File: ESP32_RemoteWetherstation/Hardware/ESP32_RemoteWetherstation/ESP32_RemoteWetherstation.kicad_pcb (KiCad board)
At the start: 2 copper layers, 48.6 x 21.9 mm, 16 parts, among them IC301 TLV77333PDBVR, J301 BOOT, J302 UART, U301 ESP32-WROOM-32E, U302 BME280

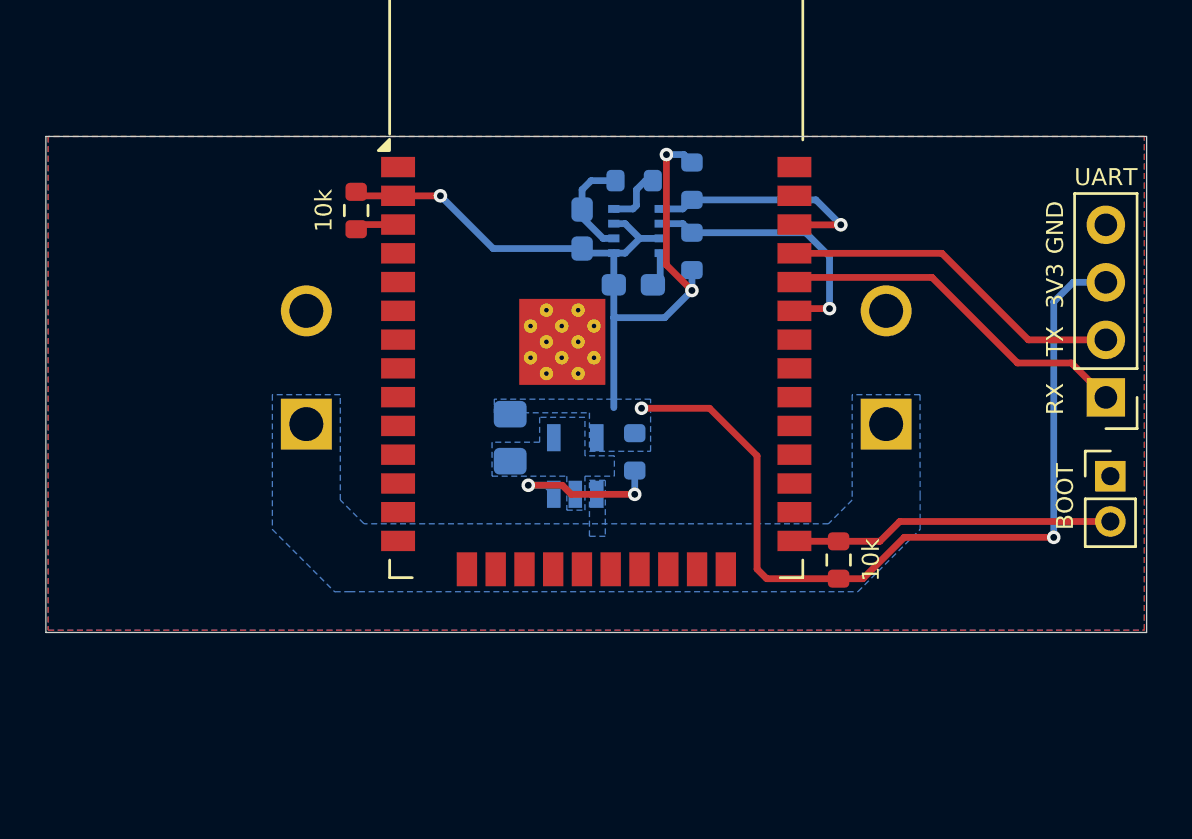
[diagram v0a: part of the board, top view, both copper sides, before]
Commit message: added IO, changed LDO
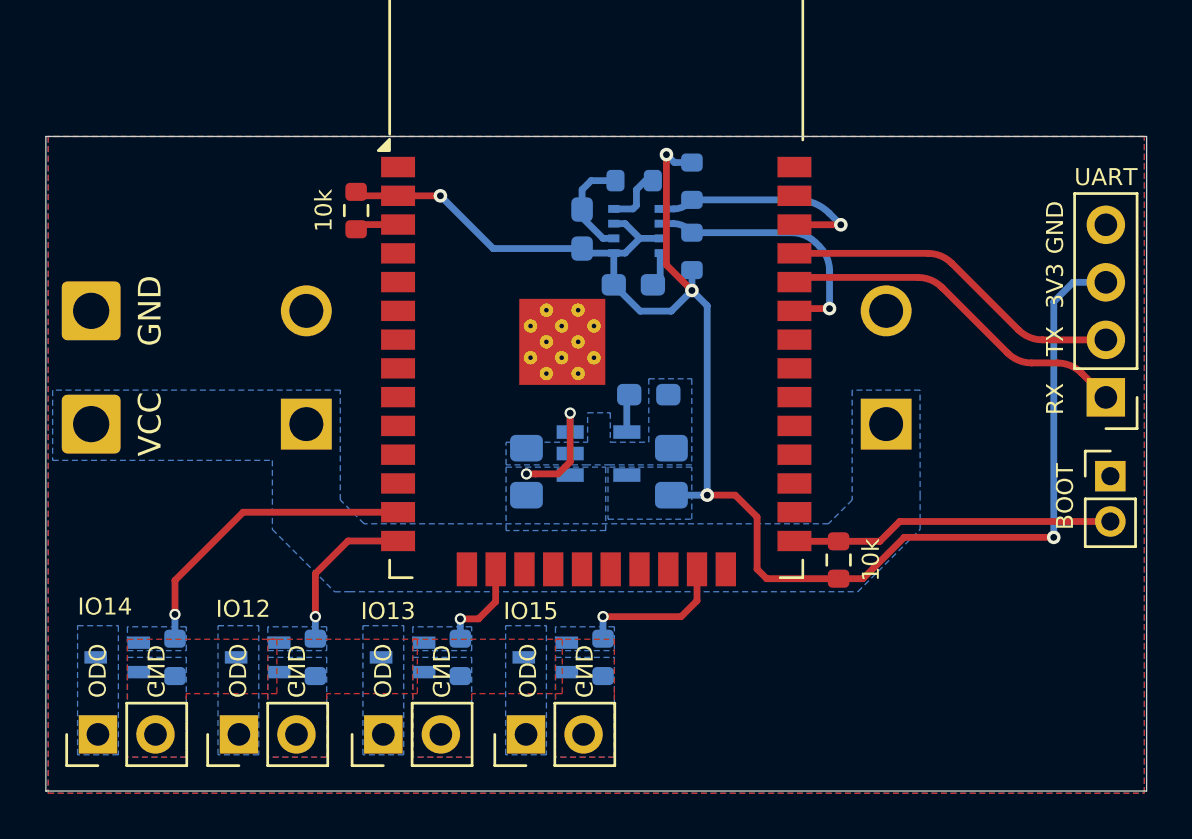
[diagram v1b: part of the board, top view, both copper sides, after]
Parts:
- removed RE_TLV301: 10k, Resistor_SMD:R_0603_1608Metric
- added C306: 1uF, Capacitor_SMD:C_0805_2012Metric_Pad1.18x1.45mm_HandSolder, B.Cu at (143.7, 65.3)
- added C307: 100pF, Capacitor_SMD:C_0603_1608Metric_Pad1.08x0.95mm_HandSolder, B.Cu at (142.7, 61.9)
- added J303: VCC, Connector_Wire:SolderWire-0.75sqmm_1x01_D1.25mm_OD2.3mm, F.Cu at (118.1, 63.2)
- added J304: GND, Connector_Wire:SolderWire-0.75sqmm_1x01_D1.25mm_OD2.3mm, F.Cu at (118.1, 58.2)
- added J305: OpenDrain, Connector_PinHeader_2.54mm:PinHeader_1x02_P2.54mm_Vertical, F.Cu at (118.4, 76.9)
- added J306: OpenDrain, Connector_PinHeader_2.54mm:PinHeader_1x02_P2.54mm_Vertical, F.Cu at (124.6, 76.9)
- added J307: OpenDrain, Connector_PinHeader_2.54mm:PinHeader_1x02_P2.54mm_Vertical, F.Cu at (131.0, 76.9)
- added J308: OpenDrain, Connector_PinHeader_2.54mm:PinHeader_1x02_P2.54mm_Vertical, F.Cu at (137.3, 76.9)
- added NT301: 0.3, Nettie_Jan:NetTie-2_SMD_Pad0.3mm, F.Cu at (138.2, 65.4)
- added Q301: NX5020UNBKWX, LibKiCad:SOT65P210X110-3N, B.Cu at (119.2, 73.5)
- added Q302: NX5020UNBKWX, LibKiCad:SOT65P210X110-3N, B.Cu at (125.5, 73.5)
- added Q303: NX5020UNBKWX, LibKiCad:SOT65P210X110-3N, B.Cu at (131.8, 73.5)
- added Q304: NX5020UNBKWX, LibKiCad:SOT65P210X110-3N, B.Cu at (138.2, 73.5)
- added R304: 100k, Resistor_SMD:R_0603_1608Metric, B.Cu at (121.8, 73.5)
- added R305: 100k, Resistor_SMD:R_0603_1608Metric, B.Cu at (128.0, 73.5)
- added R306: 100k, Resistor_SMD:R_0603_1608Metric, B.Cu at (134.4, 73.5)
- added R307: 100k, Resistor_SMD:R_0603_1608Metric, B.Cu at (140.7, 73.5)
- IC301: value TLV77333PDBVR -> AP2210K-3.3TRG1; footprint TLV77333PDBVR:SOT95P280X145-5N -> LibKiCad:SOT95P282X145-5N
- moved C305 1.66 mm to (137.3, 65.3), turned to 90 degrees
- moved IC301 1.16 mm to (140.5, 64.5), turned to 0 degrees
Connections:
- C303 pad 1: +5V -> VCC
- C304 pad 1: +5V -> VCC
- C305 pad 1: +3V3 -> VCC
- IC301 pad 1: +5V -> VCC
- IC301 pad 3: Net-(IC301-EN) -> EN
- IC301 pad 4: unconnected-(IC301-N/C-Pad4) -> BYP/ADJ
- U301 pad 13: unconnected-(U301-IO14-Pad13) -> IO14
- U301 pad 14: unconnected-(U301-IO12-Pad14) -> IO12
- U301 pad 16: unconnected-(U301-IO13-Pad16) -> IO13
- U301 pad 23: unconnected-(U301-IO15-Pad23) -> IO15
- U301 pad 27: unconnected-(U301-IO16-Pad27) -> IO16
- U301 pad 28: unconnected-(U301-IO17-Pad28) -> IO17
- U301 pad 30: unconnected-(U301-IO18-Pad30) -> IO18
- U301 pad 31: unconnected-(U301-IO19-Pad31) -> IO19
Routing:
- net IO14: track 0.00 -> 13.7 mm, vias 0 -> 1
- net Net-(IC301-EN): track 7.25 -> 0.00 mm, vias 2 -> 0
- net IO12: track 0.00 -> 7.12 mm, vias 0 -> 1
- net IO15: track 0.00 -> 6.80 mm, vias 0 -> 1
- net IO13: track 0.00 -> 4.18 mm, vias 0 -> 1
- net EN: track 0.00 -> 3.74 mm, vias 0 -> 1
- net BYP/ADJ: track 0.00 -> 1.69 mm
- net VCC: track 0.00 -> 0.40 mm, vias 0 -> 1
- added copper zone on B.Cu, net /IO/OpenDrainOutput/OpenDran
- added copper zone on B.Cu, net /IO/OpenDrainOutput1/OpenDran
- added copper zone on B.Cu, net /IO/OpenDrainOutput2/OpenDran
- added copper zone on B.Cu, net /IO/OpenDrainOutput3/OpenDran
- added copper zone on B.Cu, net IO12
- added copper zone on B.Cu, net IO13
- added copper zone on B.Cu, net IO14
- added copper zone on B.Cu, net IO15
- added copper zone on B.Cu, net VCC
- removed copper zone on B.Cu, net +5V
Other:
- board size 48.6 x 21.9 mm -> 48.6 x 28.9 mm
- board text added: "IO12"
- board text added: "IO13"
- board text added: "IO14"
- board text added: "IO15"
- board text added: "ODO"

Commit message: added Inputs
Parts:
- added J310: Analog, Connector_PinHeader_2.54mm:PinHeader_1x02_P2.54mm_Vertical, B.Cu at (155.7, 76.9)
- added J311: Analog, Connector_PinHeader_2.54mm:PinHeader_1x02_P2.54mm_Vertical, B.Cu at (149.4, 76.9)
- added J312: Analog, Connector_PinHeader_2.54mm:PinHeader_1x02_P2.54mm_Vertical, B.Cu at (162.0, 76.9)
- added R310: 6.8k, Resistor_SMD:R_0603_1608Metric, B.Cu at (156.0, 74.3)
- added R311: 1k, Resistor_SMD:R_0603_1608Metric, B.Cu at (153.0, 74.3)
- added R312: 6.8k, Resistor_SMD:R_0603_1608Metric, B.Cu at (149.7, 74.3)
- added R313: 1k, Resistor_SMD:R_0603_1608Metric, B.Cu at (146.7, 74.3)
- added R314: 6.8k, Resistor_SMD:R_0603_1608Metric, B.Cu at (162.3, 74.3)
- added R315: 1k, Resistor_SMD:R_0603_1608Metric, B.Cu at (159.2, 74.3)
- RE_ESP301: moved to B.Cu
- moved RE_ESP301 3.80 mm to (133.6, 53.9)
- moved RE_BOOT301 1.62 mm to (151.1, 67.6), turned to -90 degrees
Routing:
- net IO19: track 0.00 -> 24.3 mm, vias 0 -> 1
- net IO17: track 0.00 -> 17.0 mm, vias 0 -> 1
- net IO18: track 0.00 -> 14.9 mm, vias 0 -> 1
- net GND: track 6.18 -> 15.1 mm
- net Net-(J312-Pin_1): track 0.00 -> 3.02 mm
- net Net-(J311-Pin_1): track 0.00 -> 3.02 mm
- net Net-(J310-Pin_1): track 0.00 -> 3.02 mm
- net Net-(U301-EN): track 1.93 -> 4.19 mm, vias 0 -> 1
- net +3V3: track 73.5 -> 74.1 mm, vias 5 -> 6
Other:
- board text added: "I17"
- board text added: "I18"
- board text added: "I19"

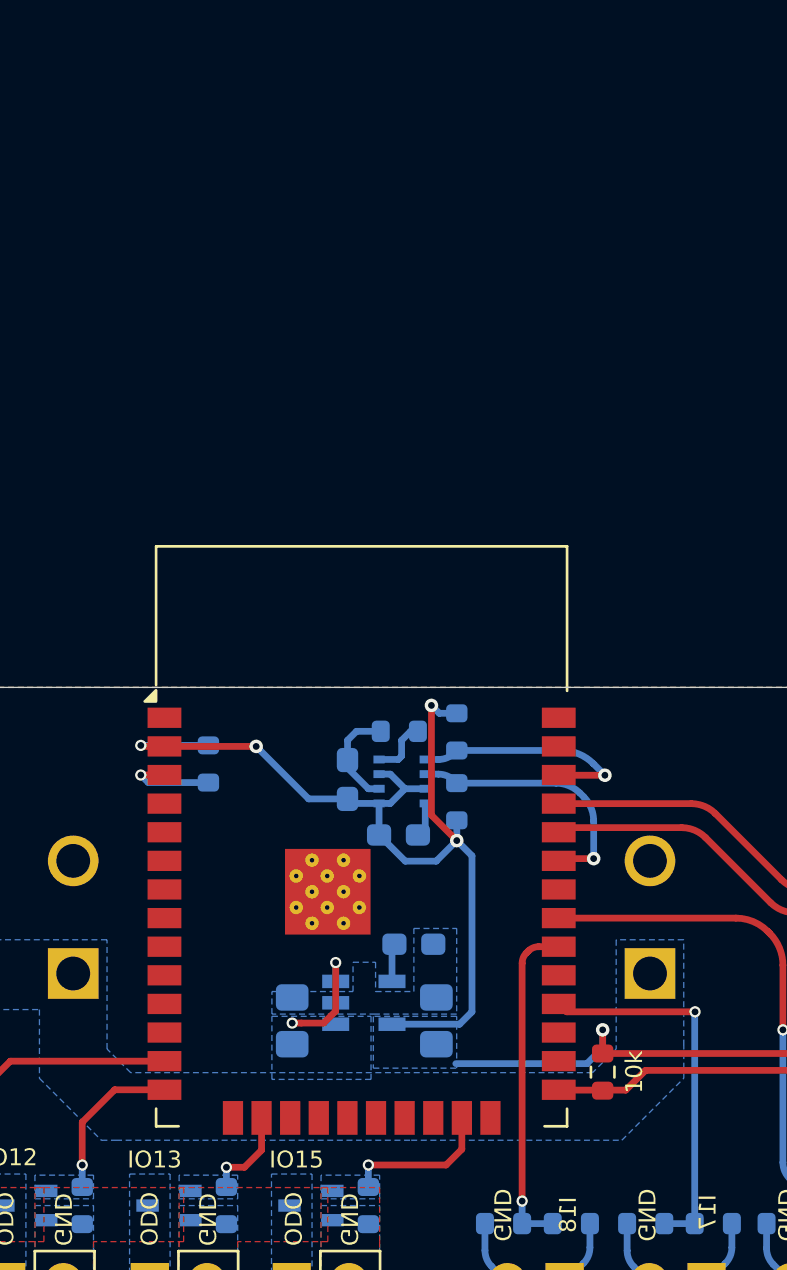
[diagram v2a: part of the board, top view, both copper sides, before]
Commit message: changed MCU
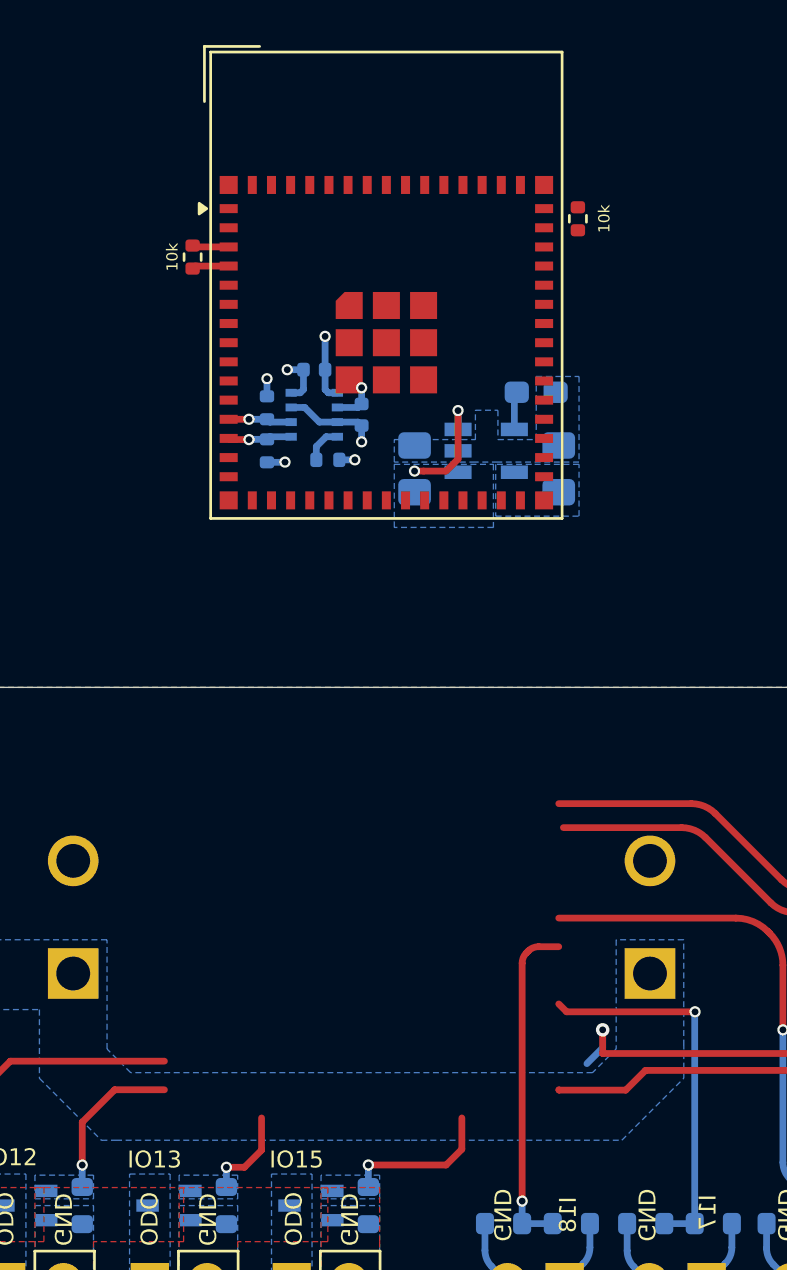
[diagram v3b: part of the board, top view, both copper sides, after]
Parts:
- removed U301: ESP32-WROOM-32E, RF_Module:ESP32-WROOM-32D
- added U303: ESP32-S3-MINI-1, RF_Module:ESP32-S2-MINI-1, F.Cu at (141.5, 32.6)
- C301, C302: footprint Capacitor_SMD:C_0603_1608Metric_Pad1.08x0.95mm_HandSolder -> Capacitor_SMD:C_0402_1005Metric
- R301, R302, R303, RE_BOOT301: footprint Resistor_SMD:R_0603_1608Metric -> Resistor_SMD:R_0402_1005Metric
- RE_ESP301: footprint Resistor_SMD:R_0603_1608Metric -> Resistor_SMD:R_0402_1005Metric; moved to F.Cu
- moved RE_BOOT301 40.5 mm to (132.9, 31.4)
- moved RE_ESP301 29.2 mm to (150.0, 29.7), turned to 90 degrees
- moved NT301 25.1 mm to (143.7, 40.9)
- moved C305 25.1 mm to (142.8, 40.8)
- moved C306 25.1 mm to (149.2, 40.8)
- moved C307 25.1 mm to (148.2, 37.4)
- moved IC301 25.1 mm to (145.9, 40.0)
- moved C301 21.0 mm to (138.3, 36.4), turned to 180 degrees
- moved R303 19.4 mm to (136.2, 38.1), turned to 90 degrees
- moved U302 16.7 mm to (138.3, 38.4), turned to -90 degrees
- moved C302 16.2 mm to (140.4, 38.4)
- moved R302 15.1 mm to (136.2, 40.0), turned to -90 degrees
- moved R301 12.5 mm to (138.9, 40.4), turned to 180 degrees
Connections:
- net IO19 renamed IO11
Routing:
- net +3V3: track 74.1 -> 34.3 mm
- net SDA: track 11.8 -> 2.83 mm
- net SCL: track 10.5 -> 2.85 mm
- net Net-(U303-EN): track 4.19 -> 0.00 mm, vias 1 -> 0
- net BOOT: track 14.3 -> 16.0 mm
- net GND: track 15.1 -> 13.7 mm, vias 0 -> 3
- net Net-(U302-SDO): track 2.65 -> 1.71 mm

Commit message: stitching/CurrentVersion
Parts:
- RE_ESP301: moved to B.Cu
- moved C305 37.3 mm to (170.1, 66.2)
- moved C306 37.3 mm to (176.5, 66.2)
- moved IC301 37.3 mm to (173.3, 65.4)
- moved C307 37.3 mm to (175.5, 62.8)
- moved NT301 37.3 mm to (171.0, 66.3)
- moved RE_ESP301 25.3 mm to (144.4, 54.4), turned to 0 degrees
- moved RE_BOOT301 25.1 mm to (134.3, 56.5)
- moved U303 25.1 mm to (142.9, 57.7)
- moved R303 21.6 mm to (142.0, 58.9), turned to 180 degrees
- moved C301 20.5 mm to (140.3, 56.8), turned to -90 degrees
- moved R302 20.4 mm to (143.9, 58.9), turned to 0 degrees
- moved U302 18.8 mm to (142.3, 56.8), turned to 0 degrees
- moved R301 17.6 mm to (144.2, 57.1), turned to 90 degrees
- moved C302 16.4 mm to (142.3, 54.7), turned to 180 degrees
- moved C303 4.40 mm to (132.0, 63.2)
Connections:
- J302 pad 1: RXD0 -> TXD0
- J302 pad 2: TXD0 -> RXD0
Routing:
- net +3V3: track 34.3 -> 51.2 mm, vias 6 -> 3
- net IO18: track 14.9 -> 2.36 mm
- net IO11: track 24.3 -> 13.2 mm
- net SCL: track 2.85 -> 12.6 mm
- net SDA: track 2.83 -> 11.2 mm
- net IO17: track 17.0 -> 10.8 mm
- net Net-(U303-EN): track 0.00 -> 5.01 mm, vias 0 -> 1
- net BOOT: track 16.0 -> 13.0 mm
- net GND: track 13.7 -> 16.0 mm, vias 3 -> 7
- net RXD0: track 15.5 -> 14.2 mm
- net TXD0: track 15.2 -> 14.0 mm

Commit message: Stitching/power module (#7)
* test: gitpush

* edited schematic looks

* deleted Backups

* StitchingPCB/try1
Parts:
- C307: footprint Capacitor_SMD:C_0603_1608Metric_Pad1.08x0.95mm_HandSolder -> Capacitor_SMD:C_0402_1005Metric
- moved NT301 6.82 mm to (168.9, 59.8), turned to 0 degrees
- moved C305 3.29 mm to (169.3, 63.0)
- moved C306 3.29 mm to (175.7, 63.0)
- moved C307 3.17 mm to (173.1, 60.7), turned to 180 degrees
- moved IC301 2.43 mm to (172.5, 63.1)
- moved RE_BOOT301 1.04 mm to (134.3, 55.4)
- moved RE_ESP301 1.04 mm to (144.4, 53.3)
- moved U303 1.04 mm to (142.9, 56.7)
- moved C301 1.04 mm to (140.2, 55.7)
- moved C302 1.04 mm to (142.2, 53.6)
- moved R301 1.04 mm to (144.1, 56.1)
- moved R302 1.04 mm to (143.8, 57.8)
- moved R303 1.04 mm to (141.9, 57.8)
- moved U302 1.04 mm to (142.2, 55.7)
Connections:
- J302 pad 1: TXD0 -> RXD0
- J302 pad 2: RXD0 -> TXD0
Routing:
- net TXD0: track 14.0 -> 28.2 mm
- net RXD0: track 14.2 -> 0.00 mm
- net EN: track 3.74 -> 0.84 mm
- net VCC: track 0.40 -> 0.00 mm, vias 1 -> 0
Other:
- board text added: "Mybe I need to change to 4 layer Gonna try switching the VCC to F.Cu, but not sure how this might help ToDo: Change VCC Layer, and check the price div. of 2-4 Layer PCB"

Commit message: stitching/PowerModule
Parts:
- moved J301 40.0 mm to (123.1, 66.3)
- moved C306 32.7 mm to (143.0, 61.8), turned to 180 degrees
- moved C307 32.6 mm to (140.7, 64.4), turned to -90 degrees
- moved NT301 29.6 mm to (140.4, 67.8), turned to -90 degrees
- moved IC301 29.5 mm to (143.1, 65.0), turned to 90 degrees
- moved C305 26.8 mm to (143.0, 68.2), turned to 180 degrees
- moved J305 12.0 mm to (117.7, 88.9)
- moved J306 12.0 mm to (123.9, 88.9)
- moved J307 12.0 mm to (130.2, 88.9)
- moved J308 12.0 mm to (136.6, 88.9)
- moved Q301 12.0 mm to (118.5, 85.5)
- moved Q302 12.0 mm to (124.7, 85.5)
- moved Q303 12.0 mm to (131.1, 85.5)
- moved Q304 12.0 mm to (137.4, 85.5)
- moved R304 12.0 mm to (121.0, 85.5)
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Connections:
- J302 pad 1: RXD0 -> TXD0
- J302 pad 2: TXD0 -> RXD0
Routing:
- net RXD0: track 0.00 -> 13.8 mm
- net TXD0: track 28.2 -> 14.5 mm
- net IO14: track 13.7 -> 0.00 mm, vias 1 -> 0
- net IO11: track 13.2 -> 1.45 mm, vias 1 -> 0
- net BOOT: track 13.0 -> 24.0 mm, vias 0 -> 1
- net IO17: track 10.8 -> 1.35 mm, vias 1 -> 0
- net IO12: track 7.12 -> 0.00 mm, vias 1 -> 0
- net +3V3: track 51.2 -> 58.2 mm
- net IO15: track 6.80 -> 0.00 mm, vias 1 -> 0
- net IO13: track 4.18 -> 0.00 mm, vias 1 -> 0
- net Net-(U303-EN): track 5.01 -> 7.69 mm
- net EN: track 0.84 -> 2.53 mm
- net IO18: track 2.36 -> 1.36 mm, vias 1 -> 0
- net SDA: track 11.2 -> 10.4 mm
- net SCL: track 12.6 -> 12.1 mm
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- added copper zone on F.Cu, net VCC
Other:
- board size 48.6 x 28.9 mm -> 43.5 x 28.3 mm
- board text added: "ToDo: Debug Leds and IO"
- board text removed: "Mybe I need to change to 4 layer Gonna try switching the VCC to F.Cu, but not sure how this might help ToDo: Change VCC Layer, and check the price div. of 2-4 Layer PCB"
